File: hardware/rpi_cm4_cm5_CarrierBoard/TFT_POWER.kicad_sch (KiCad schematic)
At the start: 78 parts, among them Q14 2N7002, Q15 2N7002, Q16 DMP3030SN-7, Q18 MMBT3904-7-F, U24 MAX16928CGUP, U25 TPS79901DRVR, U26 TPS61169DCKR, U27 AP22913W6-7

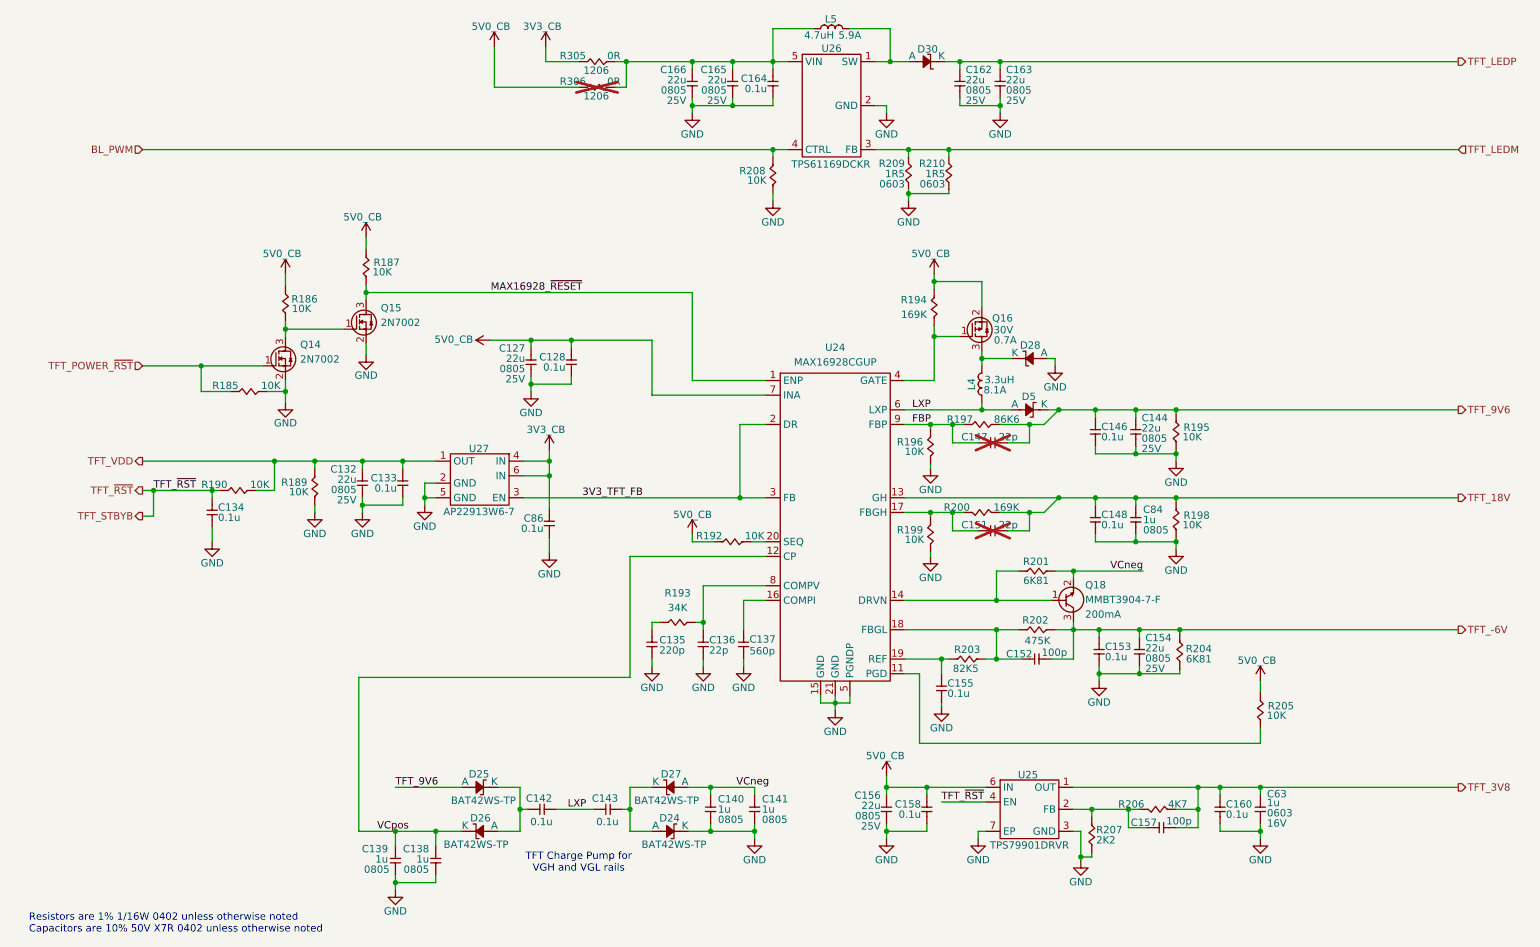
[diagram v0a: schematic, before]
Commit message: Add test points on relevant signals Re-generate SCH_PDF Re-generate BOM Re-generate all gerbers and relevant PCB output files (still in review phase)
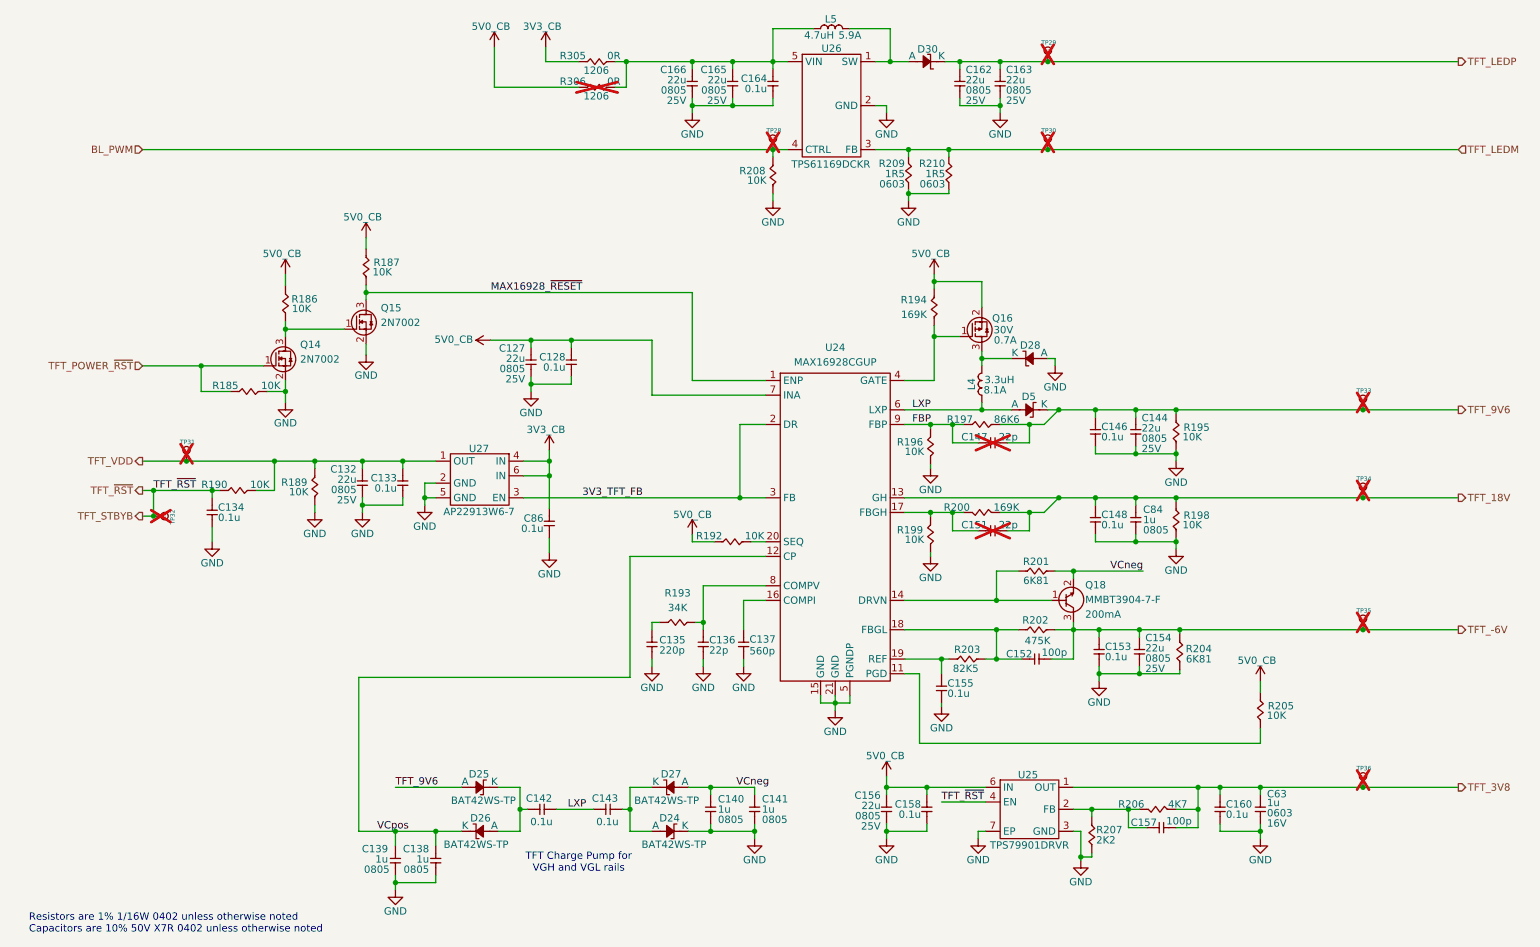
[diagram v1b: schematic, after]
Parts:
- added TP28, TP29, TP30, TP31, TP32, TP33, TP34, TP35, TP36: 28 mils, footprint:SMT_TP_28_MILS, symbol KicadCompDb:Test Point/TP_00001
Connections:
- net BL_PWM: now also TP28.1
- net TFT_-6V: now also TP35.1
- net TFT_18V: now also TP34.1
- net TFT_3V8: now also TP36.1
- net TFT_9V6: now also TP33.1
- net TFT_LEDM: now also TP30.1
- net TFT_LEDP: now also TP29.1
- net TFT_STBYB: now also TP32.1
- net TFT_VDD: now also TP31.1

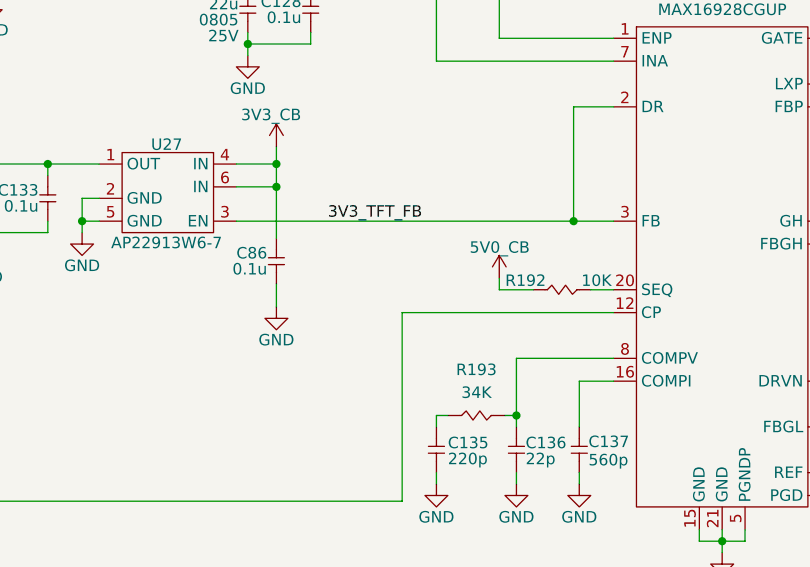
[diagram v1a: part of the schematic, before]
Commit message: Schematic review: - Add PD resistor on MAX16928 TFT driver to park TFT_VDD to OFF by default - Adjust DNP fields for PNP and standard BOM PCB review: - Add PD resistor - Adjust few traces, add missing teardrops, cleanup line segments - Regen DRC - Regen all output files
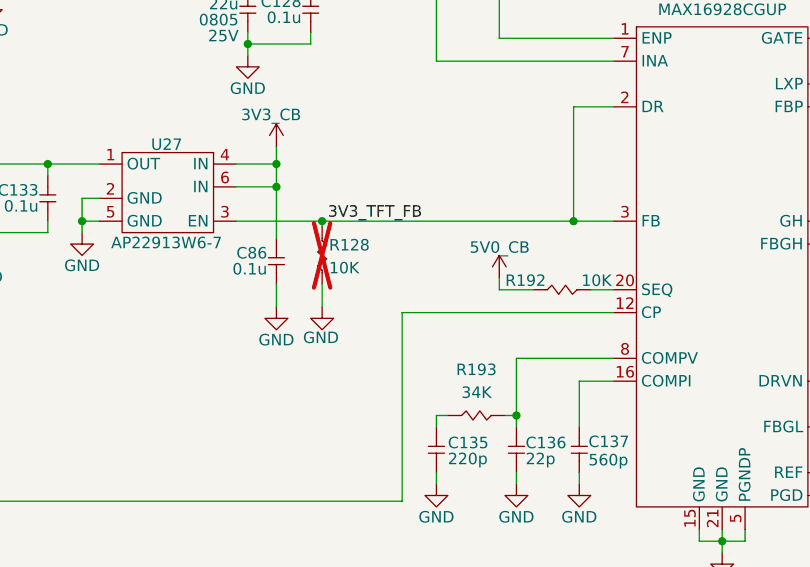
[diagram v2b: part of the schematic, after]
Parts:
- added R128: 10K, footprint:RES_0402, symbol KicadCompDb:Resistors/RES_SMT_00013
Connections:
- net 3V3_TFT_FB: now also R128.2
- net GND: now also R128.1

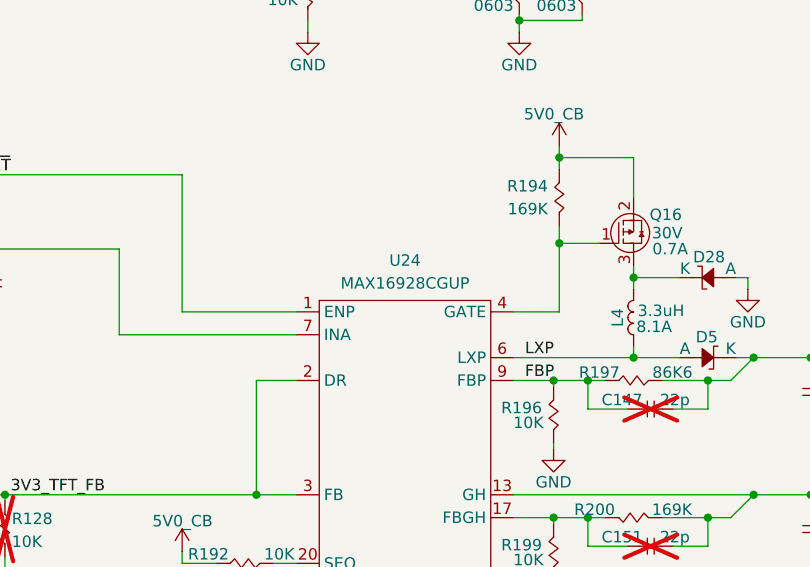
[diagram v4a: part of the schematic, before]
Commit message: Final commit prior to formal DFM by PCB manufacturer & PCBA Several iterations of DRC checks and validation with CAM software completed Ready for quotation
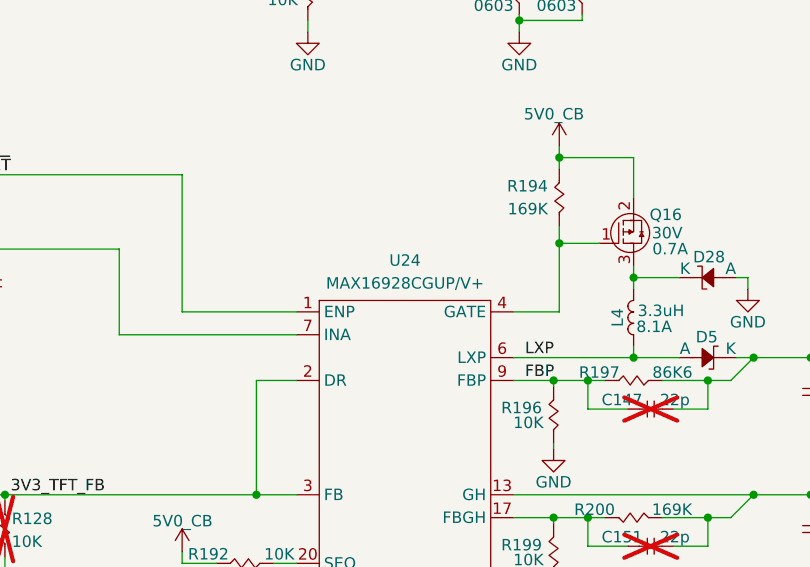
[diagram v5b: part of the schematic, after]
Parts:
- U24: value MAX16928CGUP -> MAX16928CGUP/V+
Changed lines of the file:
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@@
 	(title_block
 		(title "RPI CMx Carrier")
-		(date "2026-02-24")
+		(date "2026-02-26")
 		(rev "2.00-0A")
 		(comment 1 "Jean-Francois Bilodeau")
@@
 			)
 		)
-		(property "Value" "MAX16928CGUP"
+		(property "Value" "MAX16928CGUP/V+"
 			(at 152.4 73.66 0)
 			(effects

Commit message: Correct footprint for ENET transceiver (enlarge few holes) Correct SD card (missing 1 retaining pad) Adjust 0402 component
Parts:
- C152, C157: Dimensions 1.60mm x 0.80mm -> 1.00mm x 0.50mm; Distributor Part Number 311-1069-1-ND -> 311-1024-1-ND; Manufacturer Part Number CC0603JRNPO9BN101 -> CC0402JRNPO9BN101
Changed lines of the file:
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@@
 	(title_block
 		(title "RPI CMx Carrier")
-		(date "2026-02-28")
+		(date "2026-03-02")
 		(rev "2.00-0A")
 		(comment 1 "Jean-Francois Bilodeau")
@@
 			)
 		)
-		(property "Datasheet" "https://www.yageo.com/en/Chart/Download/pdf/CC0603JRNPO9BN101"
+		(property "Datasheet" "https://www.yageo.com/en/Chart/Download/pdf/CC0402JRNPO9BN101"
 			(at 206.375 154.305 0)
 			(effects
@@
 			)
 		)
-		(property "Description" "CAP CER 100PF 50V C0G/NPO 0603"
+		(property "Description" "CAP CER 100PF 50V C0G/NPO 0402"
 			(at 208.153 164.211 0)
 			(effects
@@
 			)
 		)
-		(property "Manufacturer Part Number" "CC0603JRNPO9BN101"
+		(property "Manufacturer Part Number" "CC0402JRNPO9BN101"
 			(at 206.629 162.179 0)
 			(effects
@@
 			)
 		)
-		(property "Distributor Part Number" "311-1069-1-ND"
+		(property "Distributor Part Number" "311-1024-1-ND"
 			(at 207.137 166.497 0)
 			(effects
@@
 			)
 		)
-		(property "Dimensions" "1.60mm x 0.80mm"
+		(property "Dimensions" "1.00mm x 0.50mm"
 			(at 206.375 154.305 0)
 			(show_name yes)
@@
 			)
 		)
-		(property "Datasheet" "https://www.yageo.com/en/Chart/Download/pdf/CC0603JRNPO9BN101"
+		(property "Datasheet" "https://www.yageo.com/en/Chart/Download/pdf/CC0402JRNPO9BN101"
 			(at 184.785 125.095 0)
 			(effects
@@
 			)
 		)
-		(property "Description" "CAP CER 100PF 50V C0G/NPO 0603"
+		(property "Description" "CAP CER 100PF 50V C0G/NPO 0402"
 			(at 186.563 135.001 0)
 			(effects
@@
 			)
 		)
-		(property "Manufacturer Part Number" "CC0603JRNPO9BN101"
+		(property "Manufacturer Part Number" "CC0402JRNPO9BN101"
 			(at 185.039 132.969 0)
 			(effects
@@
 			)
 		)
-		(property "Distributor Part Number" "311-1069-1-ND"
+		(property "Distributor Part Number" "311-1024-1-ND"
 			(at 185.547 137.287 0)
 			(effects
@@
 			)
 		)
-		(property "Dimensions" "1.60mm x 0.80mm"
+		(property "Dimensions" "1.00mm x 0.50mm"
 			(at 184.785 125.095 0)
 			(show_name yes)
